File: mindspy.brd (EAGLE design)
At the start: 68.6 x 53.3 mm, 39 parts, among them IC1 ADS1298, IC2 TPS7A4901, X1 DF9-31S, X2 STELLARIS-LAUNCHPADSTELLARIS-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

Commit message: almost final
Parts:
- added X10, X3, X5, X6, X7, X8, X9: MICRO-USB-AB-SCHIELD, molex:47589-0001
- X1: value DF9-31S -> MICRO-USB-AB-SCHIELD; device con-hirose:DF9-31S -> molex:47589-0001
- moved X1 83.9 mm to (-48.6, -5.40), turned to 0 degrees
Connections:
- net AIN1_N: now also X3.4; no longer X1.29
- net AIN1_P: now also X3.5; no longer X1.31
- net AIN2_N: now also X5.4; no longer X1.25
- net AIN2_P: now also X5.5; no longer X1.27
- net AIN3_N: now also X6.4; no longer X1.21
- net AIN3_P: now also X6.5; no longer X1.23
- net AIN4_N: now also X7.4; no longer X1.17
- net AIN4_P: now also X7.5; no longer X1.19
- net AIN5_N: now also X8.4; no longer X1.13
- net AIN5_P: now also X8.5; no longer X1.15
- net AIN6_N: now also X9.4; no longer X1.9
- net AIN6_P: now also X9.5; no longer X1.11
- net AIN7_N: now also X1.4; no longer X1.5
- net AIN7_P: now also X1.5; no longer X1.7
- net AIN8_N: now also X10.4; no longer X1.1
- net AIN8_P: now also X10.5; no longer X1.3
- net AVCM: now also X1.3, X10.3, X3.3, X5.3, X6.3, X7.3, X8.3, X9.3; no longer X1.18, X1.30
- net AVDD: now also X1.1, X10.1, X3.1, X5.1, X6.1, X7.1, X8.1, X9.1; no longer X1.20, X1.22, X1.24
- net AVSS: now also X10.2, X3.2, X5.2, X6.2, X7.2, X8.2, X9.2; no longer X1.14, X1.16, X1.4
- net RLDIN: no longer X1.8
- net RLDINV: no longer X1.10
- net RLDOUT: no longer X1.6
- net RLDREF: no longer X1.12
- net TEST_N: no longer X1.26
- net TEST_P: no longer X1.28
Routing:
- net AIN8_N: track 7.57 -> 0.00 mm
- net AIN1_P: track 7.57 -> 0.00 mm
- net AIN8_P: track 7.35 -> 0.00 mm
- net AIN1_N: track 7.35 -> 0.00 mm
- net AIN7_N: track 7.14 -> 0.00 mm
- net AIN2_P: track 7.14 -> 0.00 mm
- net AIN7_P: track 6.91 -> 0.00 mm
- net AIN2_N: track 6.91 -> 0.00 mm
- net AIN5_P: track 6.12 -> 1.89 mm
- net AIN4_N: track 6.12 -> 1.89 mm
- net AIN5_N: track 6.33 -> 2.45 mm
- net AIN4_P: track 6.33 -> 2.45 mm
- net AIN6_P: track 6.54 -> 3.04 mm
- net AIN3_N: track 6.54 -> 3.04 mm
- net AIN6_N: track 6.74 -> 3.60 mm
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
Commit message: errorneous previous commit
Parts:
- removed X10, X3, X5, X6, X7, X8, X9: MICRO-USB-AB-SCHIELD, molex:47589-0001
- added SJ6: (no value), jumper:SJ
- X1: value MICRO-USB-AB-SCHIELD -> DF9-31S; device molex:47589-0001 -> con-hirose:DF9-31S
- moved X1 84.5 mm to (27.3, 31.8), turned to 270 degrees
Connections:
- net AIN1_N: now also X1.29; no longer X3.4
- net AIN1_P: now also X1.31; no longer X3.5
- net AIN2_N: now also X1.25; no longer X5.4
- net AIN2_P: now also X1.27; no longer X5.5
- net AIN3_N: now also X1.21; no longer X6.4
- net AIN3_P: now also X1.23; no longer X6.5
- net AIN4_N: now also X1.17; no longer X7.4
- net AIN4_P: now also X1.19; no longer X7.5
- net AIN5_N: now also X1.13; no longer X8.4
- net AIN5_P: now also X1.15; no longer X8.5
- net AIN6_N: now also X1.9; no longer X9.4
- net AIN6_P: now also X1.11; no longer X9.5
- net AIN7_N: now also X1.5; no longer X1.4
- net AIN7_P: now also X1.7; no longer X1.5
- net AIN8_N: now also X1.1; no longer X10.4
- net AIN8_P: now also X1.3; no longer X10.5
- net AVCM: now also X1.22, X1.24, X1.26, X1.28, X1.30; no longer X1.3, X10.3, X3.3, X5.3, X6.3, X7.3, X8.3, X9.3
- net AVDD: now also X1.12, X1.14, X1.16, X1.18, X1.20; no longer X1.1, X10.1, X3.1, X5.1, X6.1, X7.1, X8.1, X9.1
- net AVSS: now also X1.10, X1.4, X1.6, X1.8; no longer X10.2, X3.2, X5.2, X6.2, X7.2, X8.2, X9.2
- net TEST_N: now also SJ6.1
- net TEST_P: now also SJ6.2
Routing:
- net AVDD: track 63.2 -> 91.3 mm
- net AVCM: track 13.5 -> 37.0 mm, vias 0 -> 1
- net AIN8_N: track 0.00 -> 6.94 mm
- net AIN1_P: track 0.00 -> 6.94 mm
- net AIN8_P: track 0.00 -> 6.71 mm
- net AIN1_N: track 0.00 -> 6.71 mm
- net AIN7_N: track 0.00 -> 6.50 mm
- net AIN2_P: track 0.00 -> 6.50 mm
- net AIN7_P: track 0.00 -> 6.28 mm
- net AIN2_N: track 0.00 -> 6.28 mm
- net AIN5_P: track 1.89 -> 5.49 mm
- net AIN4_N: track 1.89 -> 5.49 mm
- net AIN5_N: track 2.45 -> 5.70 mm
- net AIN4_P: track 2.45 -> 5.70 mm
- net AIN6_P: track 3.04 -> 5.90 mm
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
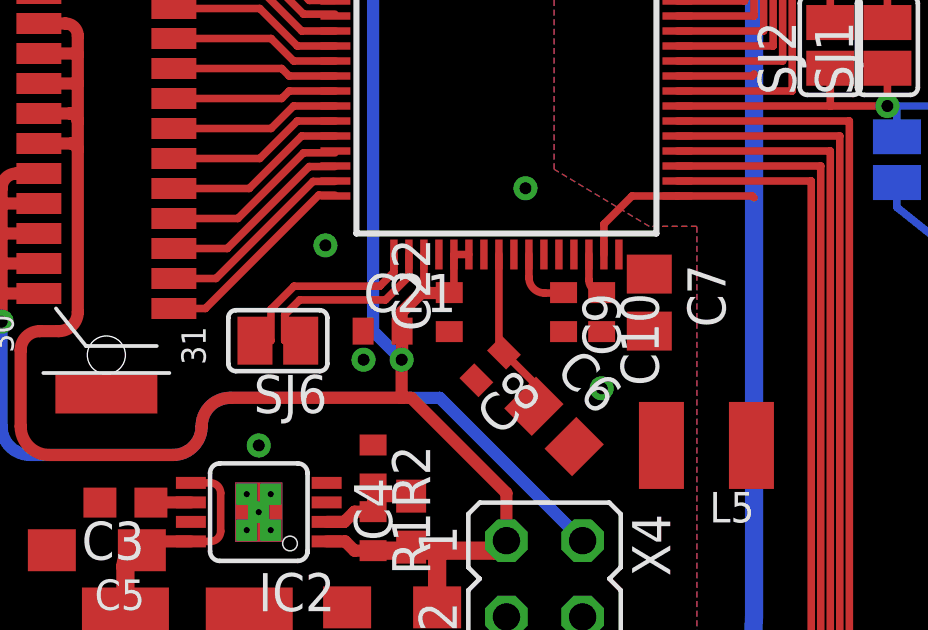
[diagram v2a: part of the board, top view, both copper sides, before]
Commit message: fix urouted capacitors C7, C9 and C10
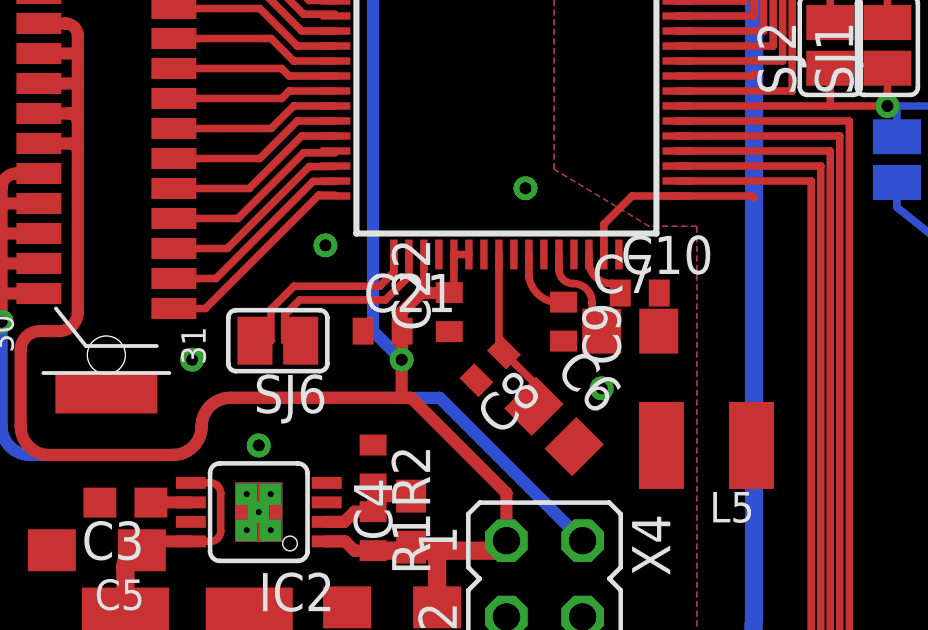
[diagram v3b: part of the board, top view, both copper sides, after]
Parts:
- moved C10 1.42 mm to (45.1, 24.8), turned to 0 degrees
- moved C7 1.14 mm to (44.8, 23.5), turned to 0 degrees
- moved C9 0.32 mm to (42.5, 23.8)
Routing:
- net N$2: track 0.00 -> 3.15 mm
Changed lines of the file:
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@@
 <element name="C5" library="rcl" package="SMC_A" value="10u" x="26.9875" y="16.1925" rot="R180"/>
 <element name="C6" library="rcl" package="C0805" value="10u" x="42.2275" y="20.32" rot="R315"/>
-<element name="C7" library="rcl" package="C0805" value="22u" x="45.4025" y="24.4475" rot="R270"/>
+<element name="C7" library="rcl" package="C0805" value="22u" x="44.7675" y="23.495"/>
 <element name="C8" library="rcl" package="C0402" value="0.1u" x="40.097990625" y="22.317990625" rot="R225"/>
-<element name="C9" library="rcl" package="C0402" value="1u" x="42.545" y="24.13" rot="R270"/>
+<element name="C9" library="rcl" package="C0402" value="1u" x="42.545" y="23.8125" rot="R270"/>
 <element name="C11" library="rcl" package="C0402" value="1n" x="35.56" y="37.465"/>
 <element name="C12" library="rcl" package="C0402" value="0.1u" x="40.3225" y="39.0525"/>
@@
 <element name="C22" library="rcl" package="C0402" value="0.1u" x="38.735" y="24.13" rot="R90"/>
 <element name="C23" library="rcl" package="C0402" value="1u" x="40.3225" y="40.005"/>
-<element name="C10" library="rcl" package="C0402" value="1u" x="43.815" y="24.13" rot="R270"/>
+<element name="C10" library="rcl" package="C0402" value="1u" x="45.085" y="24.765"/>
 <element name="X1" library="con-hirose" package="DF9-31S" value="DF9-31S" x="27.305" y="31.75" rot="R270">
 <attribute name="OC_NEWARK" value="74R3383" x="27.305" y="31.75" size="1.778" layer="27" rot="R270" display="off"/>
@@
 <wire x1="39.89" y1="37.45" x2="39.89" y2="38.835" width="0.254" layer="1"/>
 <wire x1="39.89" y1="38.835" x2="39.6725" y2="39.0525" width="0.254" layer="1"/>
-<via x="35.8775" y="22.5425" extent="1-16" drill="0.4" diameter="0.6096" shape="octagon"/>
+<via x="30.1625" y="22.5425" extent="1-16" drill="0.4" diameter="0.6096" shape="octagon"/>
 <contactref element="X1" pad="2"/>
 <contactref element="X1" pad="4"/>
@@
 <contactref element="X1" pad="8"/>
 <contactref element="X1" pad="10"/>
-<wire x1="44.39" y1="26.05" x2="43.815" y2="23.48" width="0" layer="19" extent="1-1"/>
 </signal>
 <signal name="AVDD">
@@
 <contactref element="IC1" pad="28"/>
 <contactref element="C7" pad="1"/>
-<wire x1="45.4025" y1="25.3975" x2="42.39" y2="26.05" width="0" layer="19" extent="1-1"/>
+<wire x1="42.39" y1="26.05" x2="42.39" y2="25.555" width="0.254" layer="1"/>
+<wire x1="42.39" y1="25.555" x2="42.8625" y2="25.0825" width="0.254" layer="1" curve="90"/>
+<wire x1="42.8625" y1="25.0825" x2="43.4975" y2="24.4475" width="0.254" layer="1" curve="-90"/>
+<wire x1="43.4975" y1="24.4475" x2="43.4975" y2="24.13" width="0.254" layer="1"/>
+<wire x1="43.4975" y1="24.13" x2="43.8175" y2="23.81" width="0.254" layer="1" curve="-90"/>
+<wire x1="43.8175" y1="23.81" x2="43.8175" y2="23.495" width="0.254" layer="1"/>
 </signal>
 <signal name="N$1">
@@
 <contactref element="IC1" pad="26"/>
 <contactref element="C9" pad="1"/>
-<wire x1="41.39" y1="26.05" x2="41.39" y2="25.285" width="0.254" layer="1"/>
-<wire x1="41.39" y1="25.285" x2="41.91" y2="24.765" width="0.254" layer="1" curve="90"/>
-<wire x1="41.91" y1="24.765" x2="42.53" y2="24.765" width="0.254" layer="1"/>
-<wire x1="42.53" y1="24.765" x2="42.545" y2="24.78" width="0.254" layer="1" curve="90"/>
+<wire x1="41.39" y1="26.05" x2="41.39" y2="25.3" width="0.254" layer="1"/>
+<wire x1="41.39" y1="25.3" x2="42.545" y2="24.4625" width="0.254" layer="1" curve="90"/>
 </signal>
 <signal name="N$5">
 <contactref element="IC1" pad="30"/>
 <contactref element="C10" pad="1"/>
-<wire x1="43.39" y1="26.05" x2="43.39" y2="25.205" width="0.254" layer="1"/>
-<wire x1="43.39" y1="25.205" x2="43.815" y2="24.78" width="0.254" layer="1" curve="90"/>
+<wire x1="43.39" y1="26.05" x2="43.39" y2="25.825" width="0.254" layer="1"/>
+<wire x1="43.39" y1="25.825" x2="44.1325" y2="25.0825" width="0.254" layer="1" curve="90"/>
+<wire x1="44.1325" y1="25.0825" x2="44.45" y2="25.0675" width="0.254" layer="1"/>
+<wire x1="44.45" y1="25.0675" x2="44.435" y2="24.765" width="0.254" layer="1" curve="90"/>
 </signal>
 <signal name="N$6">

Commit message: .
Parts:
- removed L3: 10u, fabhack:L1210K
- moved C9 2.54 mm to (42.5, 21.3), turned to 315 degrees
- moved C7 1.61 mm to (43.4, 22.6), turned to 315 degrees
- moved L5 1.59 mm to (47.3, 18.1)
- moved C10 1.31 mm to (44.8, 23.5), turned to 315 degrees
- moved C6 0.95 mm to (41.3, 20.3)
- moved C8 0.71 mm to (39.5, 22.0)
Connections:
- net AVSS: no longer L3.2
- net DGND: no longer L3.1
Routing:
- net N$4: track 2.18 -> 4.61 mm
- net AVCM: track 37.0 -> 34.8 mm
- net DGND: track 12.0 -> 13.2 mm, vias 8 -> 10
- net N$5: track 1.90 -> 2.48 mm
- net AVDD: track 91.3 -> 90.8 mm

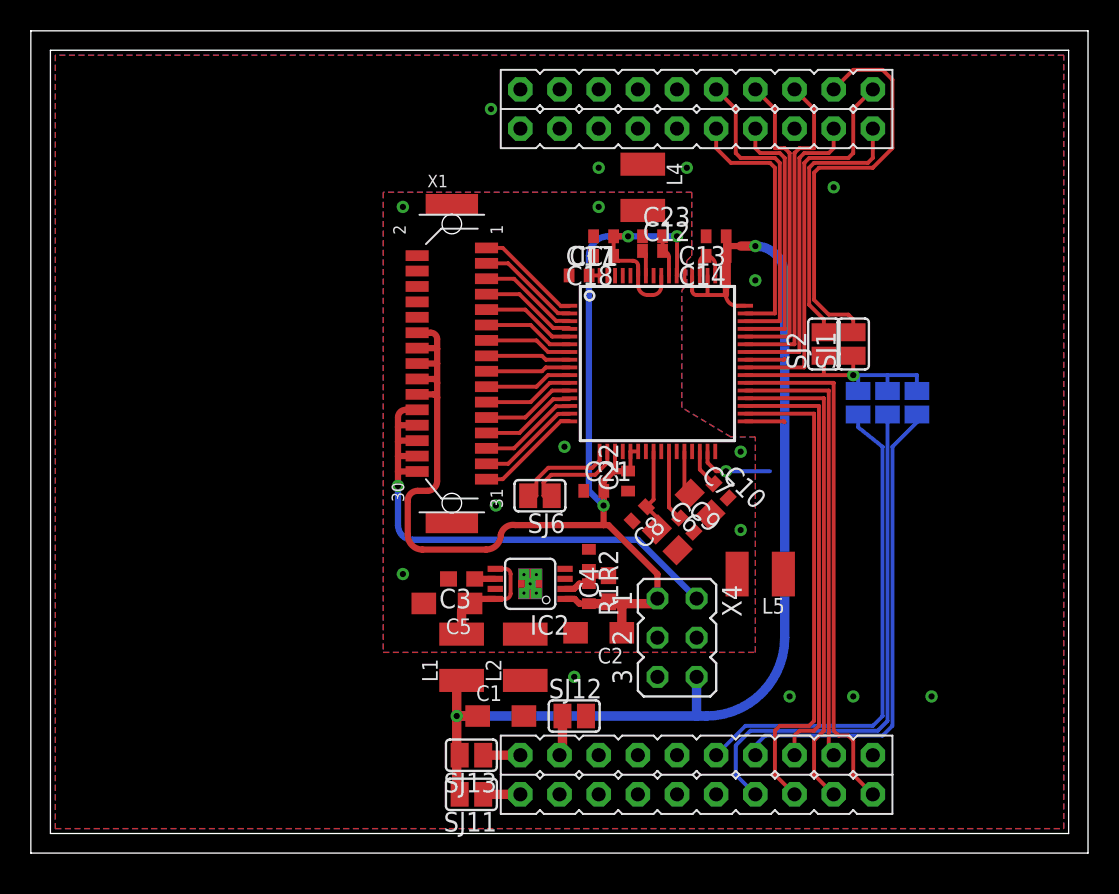
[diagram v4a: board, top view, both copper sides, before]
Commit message: use half-sized launchpad shield
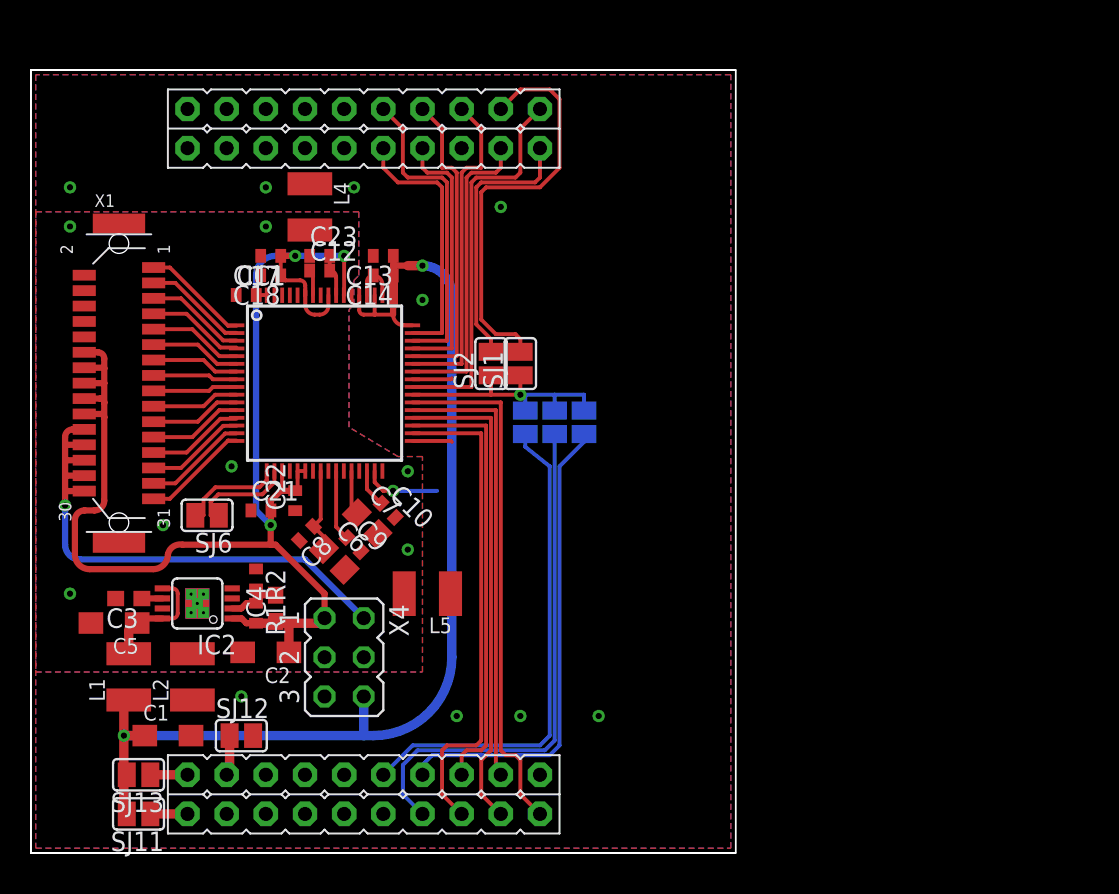
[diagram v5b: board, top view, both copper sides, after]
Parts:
- X2: value STELLARIS-LAUNCHPADSTELLARIS-LAUNCHPAD -> STELLARIS-LAUNCHPAD-HALF; device fabhack:LAUNCHPAD-XL -> ti:LAUNCHPAD-L
- moved C11 21.6 mm to (14.0, 36.2)
- moved C13 21.6 mm to (22.9, 38.7)
- moved C14 21.6 mm to (22.9, 37.5)
- moved C17 21.6 mm to (15.6, 38.7)
- moved C18 21.6 mm to (15.6, 37.5)
- moved C21 21.6 mm to (14.9, 22.2)
- moved C3 21.6 mm to (6.35, 16.5)
- moved C4 21.6 mm to (15.9, 15.9)
- moved C8 21.6 mm to (17.9, 20.7)
- moved C9 21.6 mm to (21.0, 20.0)
- moved L1 21.6 mm to (6.35, 11.4)
- moved L2 21.6 mm to (10.5, 11.4)
- moved SJ1 21.6 mm to (31.8, 31.8)
- moved SJ2 21.6 mm to (29.8, 31.8)
- moved SJ3 21.6 mm to (35.9, 27.9)
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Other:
- board size 68.6 x 53.3 mm -> 45.7 x 50.8 mm
